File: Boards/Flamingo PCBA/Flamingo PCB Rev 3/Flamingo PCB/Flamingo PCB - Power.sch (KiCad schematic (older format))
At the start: 33 parts, among them J401 10103594-0001LF, J402 JST PH Battery Connector, J403 Wire Switch Here, Q401 P-Channel 1.25-W MOSFET, U401 3.3V_Reg, U402 3.3V_Reg, U403 LiPo Charger 500 mA, U404 1.8V_Reg, U405 1.8V_Reg

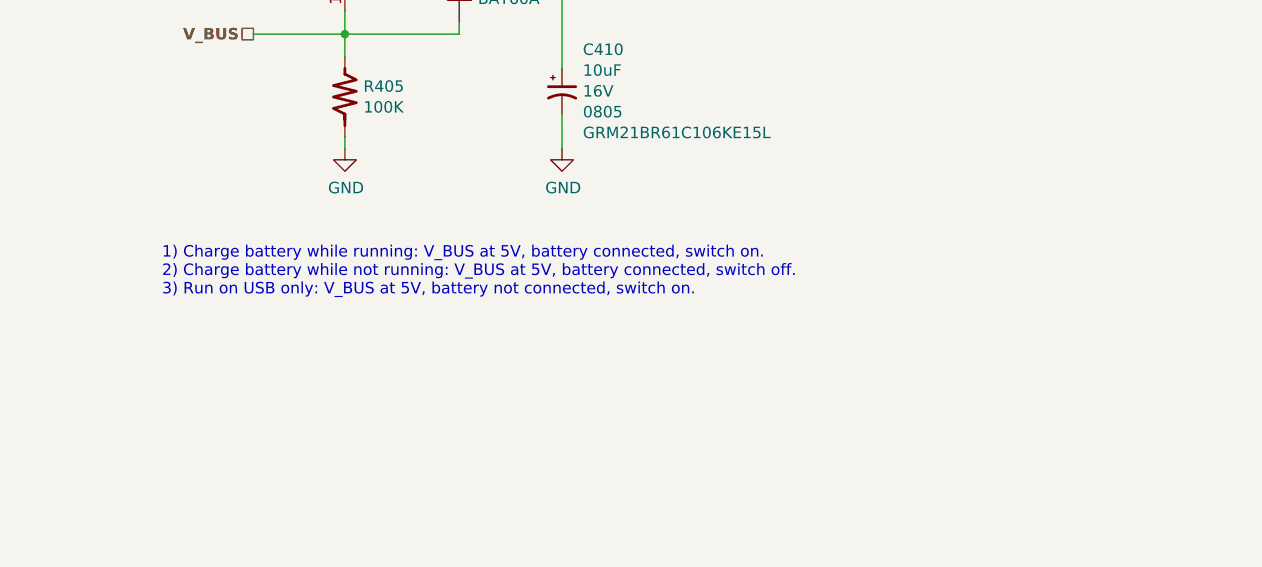
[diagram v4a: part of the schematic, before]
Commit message: More work on Arduino sheet
Added V_BUS sensing, removed V_BAT sensing bc it would be a discharge situation. Assigned some lines to pins. Added placeholders for headers.
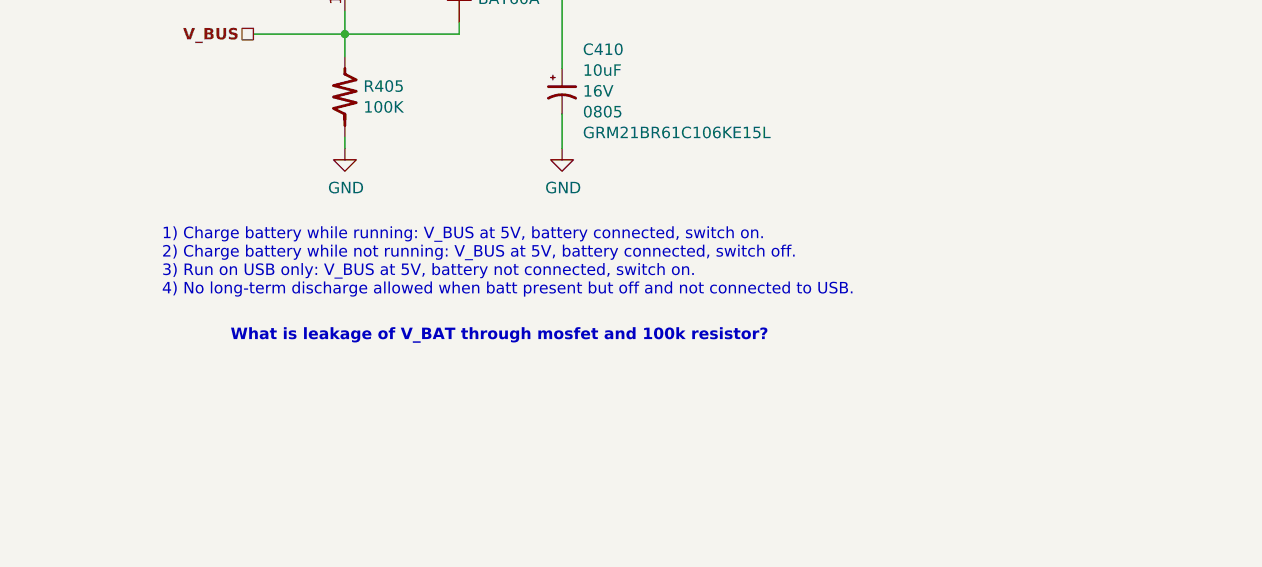
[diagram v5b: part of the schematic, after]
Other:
- note added: "1) Charge battery while running: V_BUS at 5V, battery connected, switch on.\n2) Charge battery while not running: V_BUS at 5V, battery connected, switch off.\n3) Run on USB only: V_BUS at 5V, battery not connected, switch on.\n4) No long-term discharge allowed when batt present but off and not connected to USB."
- note added: "What is leakage of V_BAT through mosfet and 100k resistor?"
- note removed: "1) Charge battery while running: V_BUS at 5V, battery connected, switch on.\n2) Charge battery while not running: V_BUS at 5V, battery connected, switch off.\n3) Run on USB only: V_BUS at 5V, battery not connected, switch on."
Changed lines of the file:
@@
 	5350 1750 6150 1750
 Text Notes 7450 3300 0    50   ~ 0
-1) Charge battery while running: V_BUS at 5V, battery connected, switch on.\n2) Charge battery while not running: V_BUS at 5V, battery connected, switch off.\n3) Run on USB only: V_BUS at 5V, battery not connected, switch on.
+1) Charge battery while running: V_BUS at 5V, battery connected, switch on.\n2) Charge battery while not running: V_BUS at 5V, battery connected, switch off.\n3) Run on USB only: V_BUS at 5V, battery not connected, switch on.\n4) No long-term discharge allowed when batt present but off and not connected to USB.
 Text Notes 2000 6500 0    50   ~ 0
 Datasheet suggests a Schottky to avoid reverse biasing Vin/Vout if that is a possibility but I don't expect that to happen.
@@
 Text Notes 2400 1500 0    50   ~ 0
 V_BUS also comes\nfrom the UART header
+Text Notes 7750 3500 0    50   ~ 10
+What is leakage of V_BAT through mosfet and 100k resistor?
 $EndSCHEMATC

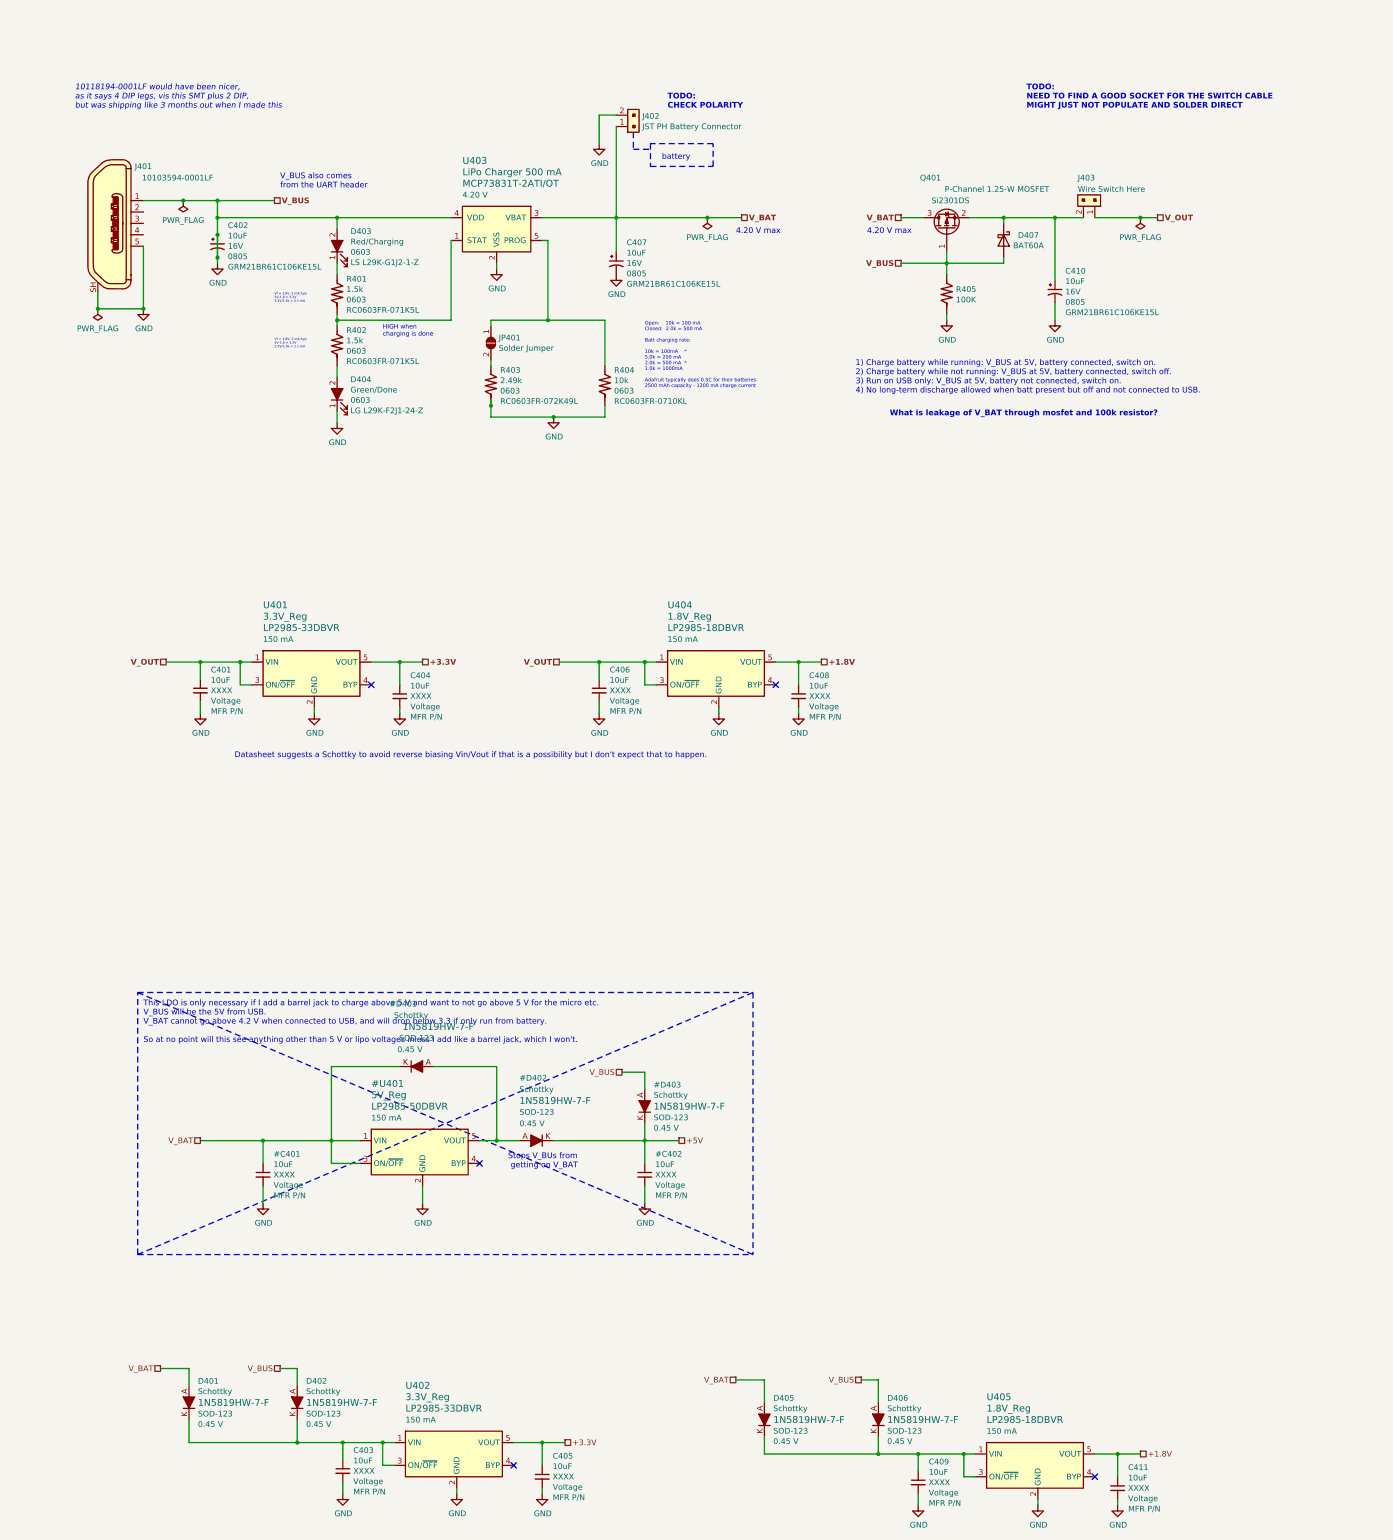
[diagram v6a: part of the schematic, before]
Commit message: Wired up top-level sheet, fixed some hier. pins
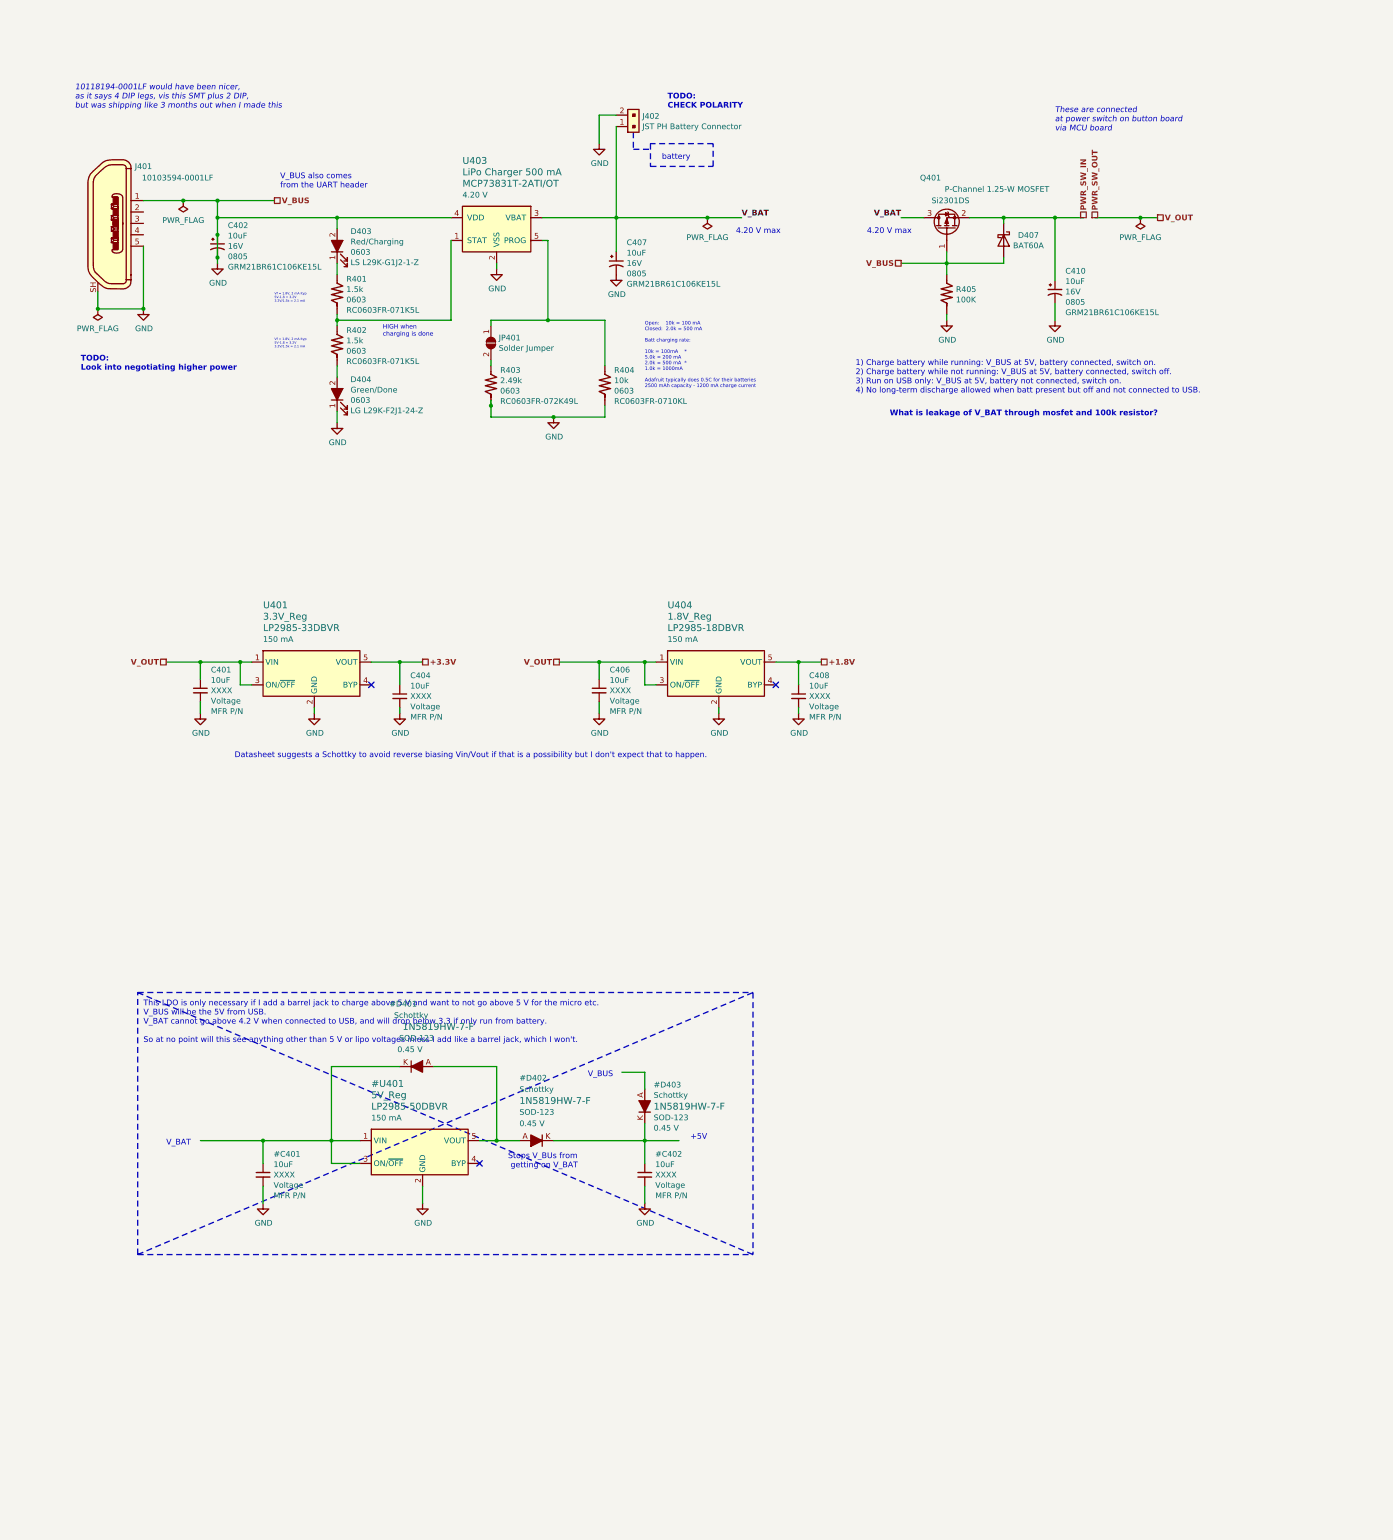
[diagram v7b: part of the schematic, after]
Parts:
- removed C403, C405, C409, C411: 10uF, symbol MyCapacitors:C_Small_vert
- removed D401, D402, D405, D406: Schottky, digikey-footprints:SOD-123, symbol dk_Diodes-Rectifiers-Single:1N5819HW-7-F
- removed J403: Wire Switch Here, digikey-footprints:PinHeader_1x2_P2mm_Drill1mm_RA, symbol dk_Rectangular-Connectors-Headers-Male-Pins:S2B-PH-K-S_LF__SN_
- removed U402: 3.3V_Reg, digikey-footprints:SOT-753, symbol MyICs:3.3V_Reg
- removed U405: 1.8V_Reg, digikey-footprints:SOT-753, symbol MyICs:3.3V_Reg
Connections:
- net labels added: PWR_SW_IN, PWR_SW_OUT
- net labels removed: +5V
- wire segments 138 -> 100
- no-connect marks 5 -> 3
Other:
- note added: "+5V"
- note added: "TODO:\nLook into negotiating higher power"
- note added: "These are connected \nat power switch on button board\nvia MCU board"
- note added: "V_BAT"
- note added: "V_BUS"
- note removed: "TODO:\nNEED TO FIND A GOOD SOCKET FOR THE SWITCH CABLE\nMIGHT JUST NOT POPULATE AND SOLDER DIRECT"

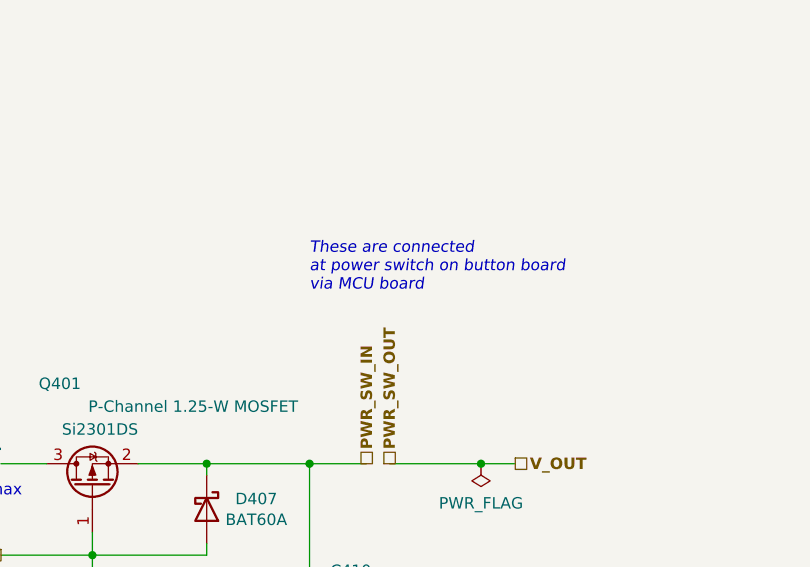
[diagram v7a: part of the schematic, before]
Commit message: Added Button Remote project
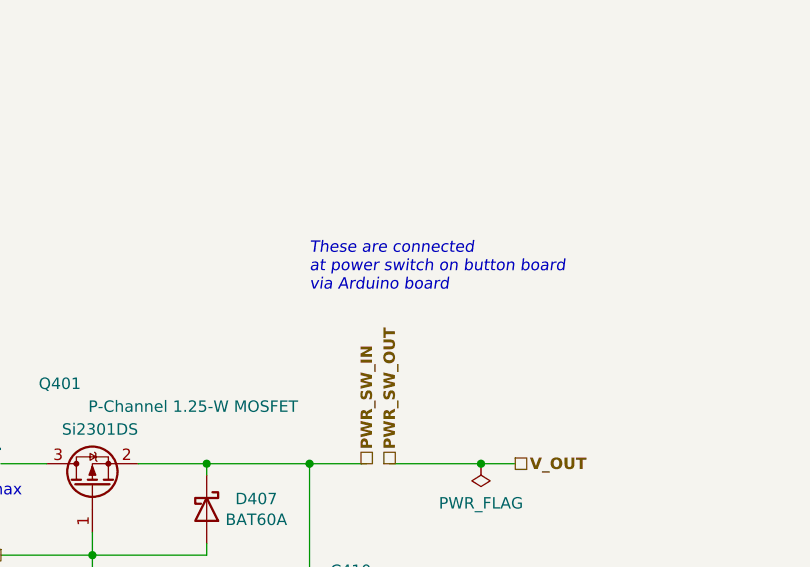
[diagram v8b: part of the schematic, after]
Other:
- note added: "These are connected \nat power switch on button board\nvia Arduino board"
- note removed: "These are connected \nat power switch on button board\nvia MCU board"
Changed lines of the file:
@@
 $Descr A4 11693 8268
 encoding utf-8
-Sheet 2 5
+Sheet 2 4
 Title ""
 Date ""
@@
 V_BAT
 Text Notes 9200 1000 0    50   Italic 0
-These are connected \nat power switch on button board\nvia MCU board
+These are connected \nat power switch on button board\nvia Arduino board
 $EndSCHEMATC
